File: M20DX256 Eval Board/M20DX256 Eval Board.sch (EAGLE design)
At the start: 20 parts, among them J1 M52-040000S0545, J2 20_PIN, J3 20_PIN, SW1 KMR211G, U1 MK20DX256VLH7, Y1 8MHz, Y2 32.768kHz, 12.5pF

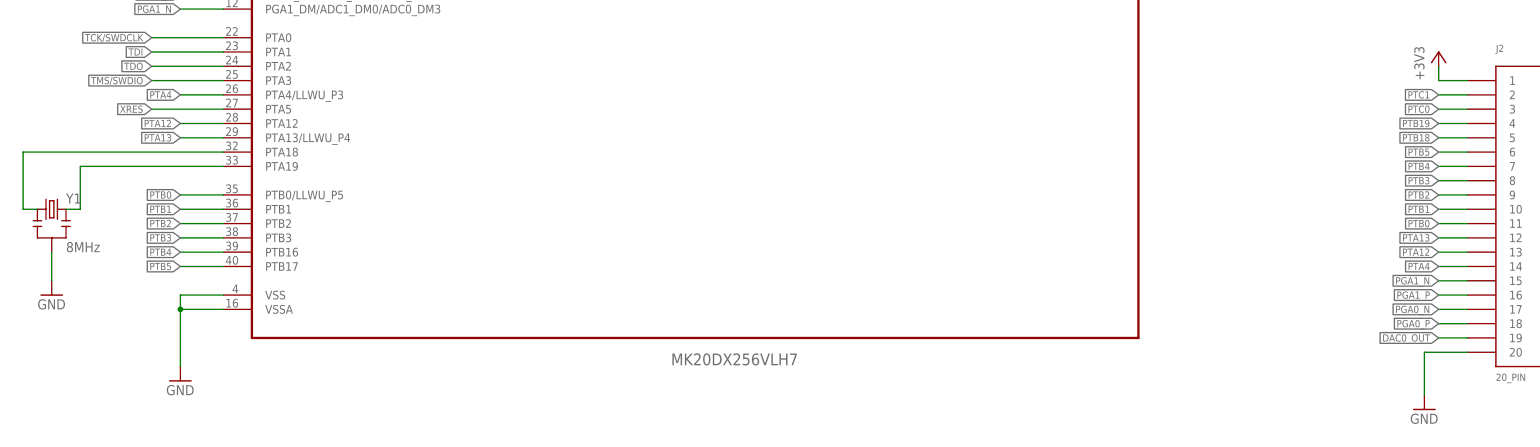
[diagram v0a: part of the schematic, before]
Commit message: Place the component on the board
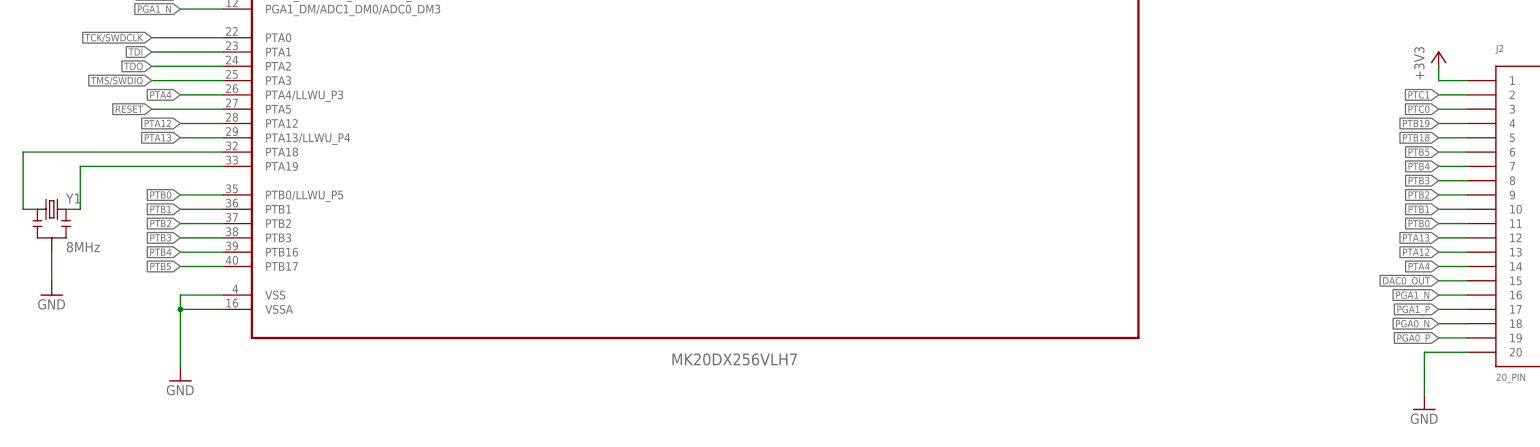
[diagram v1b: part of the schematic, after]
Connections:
- removed net XRES: U1A.PTA5
- net DAC0_OUT: now also J2.15; no longer J2.19
- net PGA0_N: now also J2.18; no longer J2.17
- net PGA0_P: now also J2.19; no longer J2.18
- net PGA1_N: now also J2.16; no longer J2.15
- net PGA1_P: now also J2.17; no longer J2.16
- net RESET: now also U1A.PTA5
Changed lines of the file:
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@@
-</segment>
-</net>
-<net name="XRES" class="0">
-<segment>
-<pinref part="U1" gate="A" pin="PTA5"/>
-<wire x1="137.16" y1="185.42" x2="124.46" y2="185.42" width="0.1524" layer="91"/>
-<label x="124.46" y="185.42" size="1.27" layer="95" rot="R180" xref="yes"/>
 </segment>
 </net>
@@
 </segment>
 <segment>
-<wire x1="358.14" y1="154.94" x2="353.06" y2="154.94" width="0.1524" layer="91"/>
-<label x="353.06" y="154.94" size="1.27" layer="95" rot="R180" xref="yes"/>
-<pinref part="J2" gate="G$1" pin="15"/>
+<wire x1="358.14" y1="152.4" x2="353.06" y2="152.4" width="0.1524" layer="91"/>
+<label x="353.06" y="152.4" size="1.27" layer="95" rot="R180" xref="yes"/>
+<pinref part="J2" gate="G$1" pin="16"/>
 </segment>
 </net>
@@
 </segment>
 <segment>
-<wire x1="358.14" y1="152.4" x2="353.06" y2="152.4" width="0.1524" layer="91"/>
-<label x="353.06" y="152.4" size="1.27" layer="95" rot="R180" xref="yes"/>
-<pinref part="J2" gate="G$1" pin="16"/>
+<wire x1="358.14" y1="149.86" x2="353.06" y2="149.86" width="0.1524" layer="91"/>
+<label x="353.06" y="149.86" size="1.27" layer="95" rot="R180" xref="yes"/>
+<pinref part="J2" gate="G$1" pin="17"/>
 </segment>
 </net>
@@
 </segment>
 <segment>
-<wire x1="358.14" y1="149.86" x2="353.06" y2="149.86" width="0.1524" layer="91"/>
-<label x="353.06" y="149.86" size="1.27" layer="95" rot="R180" xref="yes"/>
-<pinref part="J2" gate="G$1" pin="17"/>
+<wire x1="358.14" y1="147.32" x2="353.06" y2="147.32" width="0.1524" layer="91"/>
+<label x="353.06" y="147.32" size="1.27" layer="95" rot="R180" xref="yes"/>
+<pinref part="J2" gate="G$1" pin="18"/>
 </segment>
 </net>
@@
 </segment>
 <segment>
-<wire x1="358.14" y1="147.32" x2="353.06" y2="147.32" width="0.1524" layer="91"/>
-<label x="353.06" y="147.32" size="1.27" layer="95" rot="R180" xref="yes"/>
-<pinref part="J2" gate="G$1" pin="18"/>
+<wire x1="358.14" y1="144.78" x2="353.06" y2="144.78" width="0.1524" layer="91"/>
+<label x="353.06" y="144.78" size="1.27" layer="95" rot="R180" xref="yes"/>
+<pinref part="J2" gate="G$1" pin="19"/>
 </segment>
 </net>
@@
 <label x="347.98" y="226.06" size="1.27" layer="95" rot="R180" xref="yes"/>
 </segment>
+<segment>
+<pinref part="U1" gate="A" pin="PTA5"/>
+<wire x1="137.16" y1="185.42" x2="124.46" y2="185.42" width="0.1524" layer="91"/>
+<label x="124.46" y="185.42" size="1.27" layer="95" rot="R180" xref="yes"/>
+</segment>
 </net>
 <net name="N$7" class="0">
@@
 </segment>
 <segment>
-<pinref part="J2" gate="G$1" pin="19"/>
-<wire x1="358.14" y1="144.78" x2="353.06" y2="144.78" width="0.1524" layer="91"/>
-<label x="353.06" y="144.78" size="1.27" layer="95" rot="R180" xref="yes"/>
-</segment>
-</net>
+<wire x1="358.14" y1="154.94" x2="353.06" y2="154.94" width="0.1524" layer="91"/>
+<label x="353.06" y="154.94" size="1.27" layer="95" rot="R180" xref="yes"/>
+<pinref part="J2" gate="G$1" pin="15"/>
+</segment>
+</net>

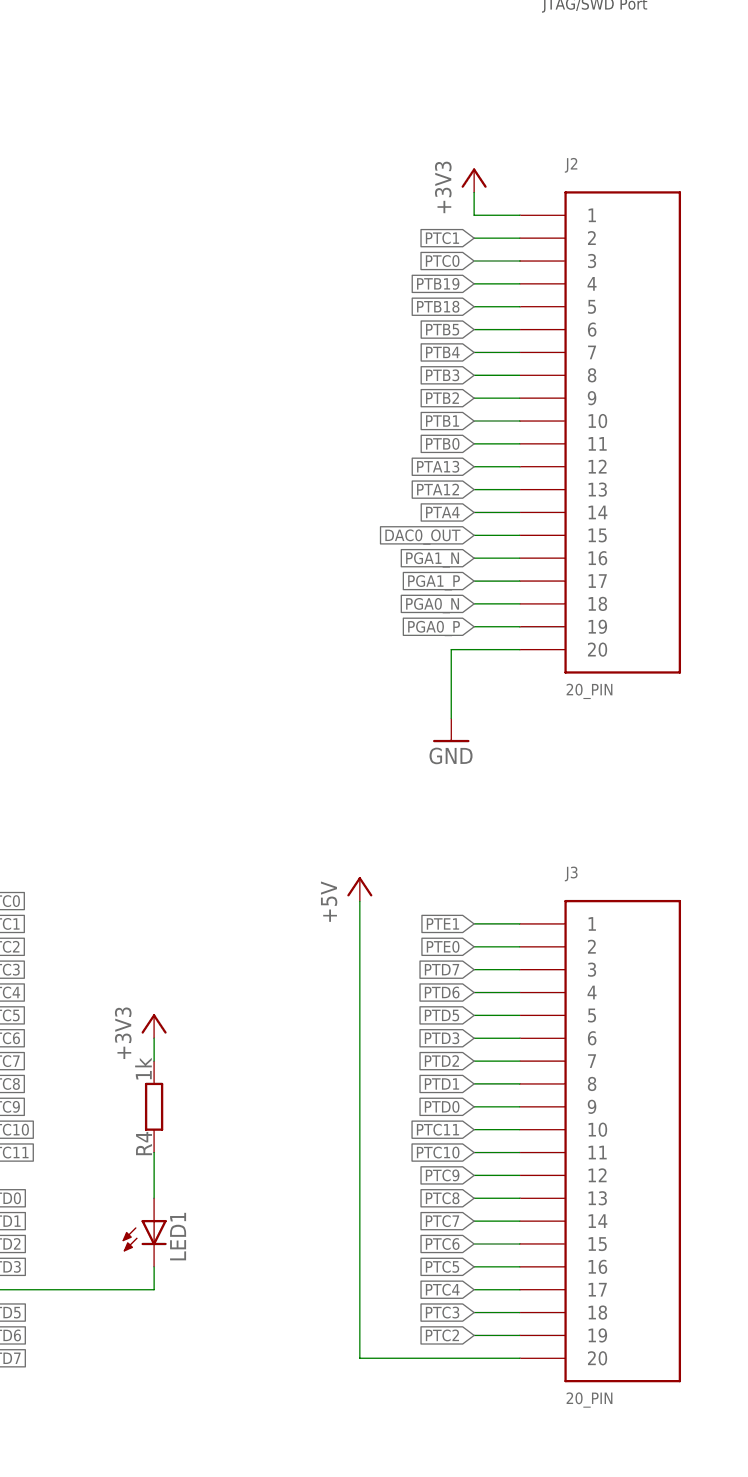
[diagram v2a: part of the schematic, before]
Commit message: Route the power supply +5V
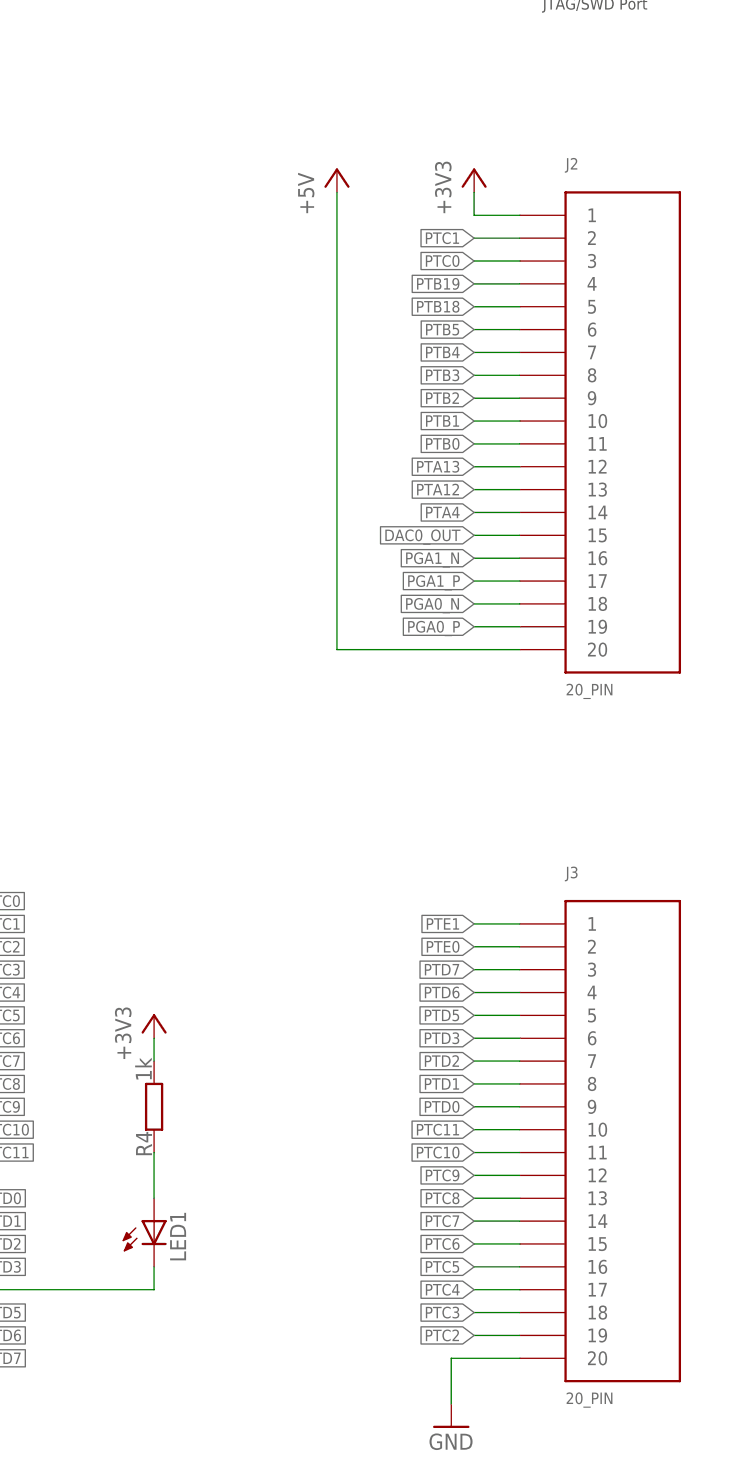
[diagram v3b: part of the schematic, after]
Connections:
- net +5V: now also J2.20; no longer J3.20
- net GND: now also J3.20; no longer J2.20
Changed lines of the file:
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@@
 <part name="J3" library="con-custom" deviceset="20_PIN" device=""/>
 <part name="+3V8" library="supply1" deviceset="+3V3" device=""/>
-<part name="P+3" library="supply1" deviceset="+5V" device=""/>
-<part name="GND8" library="supply1" deviceset="GND" device=""/>
 <part name="R3" library="rcl" deviceset="R-EU_" device="R0603" value="10k"/>
 <part name="C7" library="rcl" deviceset="C-EU" device="C0603" value="0.1uF"/>
@@
 <part name="R4" library="rcl" deviceset="R-EU_" device="R0603" value="1k"/>
 <part name="+3V10" library="supply1" deviceset="+3V3" device=""/>
+<part name="GND11" library="supply1" deviceset="GND" device=""/>
+<part name="P+4" library="supply1" deviceset="+5V" device=""/>
 </parts>
 <sheets>
@@
 <instance part="J3" gate="G$1" x="370.84" y="88.9"/>
 <instance part="+3V8" gate="G$1" x="353.06" y="195.58"/>
-<instance part="P+3" gate="1" x="340.36" y="116.84"/>
-<instance part="GND8" gate="1" x="350.52" y="132.08"/>
 <instance part="R3" gate="G$1" x="15.24" y="165.1" rot="R90"/>
 <instance part="C7" gate="G$1" x="15.24" y="152.4"/>
@@
 </instance>
 <instance part="+3V10" gate="G$1" x="317.5" y="101.6"/>
+<instance part="GND11" gate="1" x="350.52" y="55.88"/>
+<instance part="P+4" gate="1" x="337.82" y="195.58"/>
 </instances>
 <busses>
@@
 </segment>
 <segment>
-<pinref part="GND8" gate="1" pin="GND"/>
-<wire x1="350.52" y1="134.62" x2="350.52" y2="142.24" width="0.1524" layer="91"/>
-<pinref part="J2" gate="G$1" pin="20"/>
-<wire x1="350.52" y1="142.24" x2="358.14" y2="142.24" width="0.1524" layer="91"/>
-</segment>
-<segment>
 <pinref part="C7" gate="G$1" pin="2"/>
 <pinref part="GND9" gate="1" pin="GND"/>
@@
 <pinref part="GND10" gate="1" pin="GND"/>
 </segment>
+<segment>
+<pinref part="J3" gate="G$1" pin="20"/>
+<pinref part="GND11" gate="1" pin="GND"/>
+<wire x1="358.14" y1="63.5" x2="350.52" y2="63.5" width="0.1524" layer="91"/>
+<wire x1="350.52" y1="63.5" x2="350.52" y2="58.42" width="0.1524" layer="91"/>
+</segment>
 </net>
 <net name="+5V" class="0">
@@
 </segment>
 <segment>
-<pinref part="P+3" gate="1" pin="+5V"/>
-<wire x1="340.36" y1="114.3" x2="340.36" y2="63.5" width="0.1524" layer="91"/>
-<pinref part="J3" gate="G$1" pin="20"/>
-<wire x1="358.14" y1="63.5" x2="340.36" y2="63.5" width="0.1524" layer="91"/>
+<pinref part="J2" gate="G$1" pin="20"/>
+<pinref part="P+4" gate="1" pin="+5V"/>
+<wire x1="358.14" y1="142.24" x2="337.82" y2="142.24" width="0.1524" layer="91"/>
+<wire x1="337.82" y1="142.24" x2="337.82" y2="193.04" width="0.1524" layer="91"/>
 </segment>
 </net>

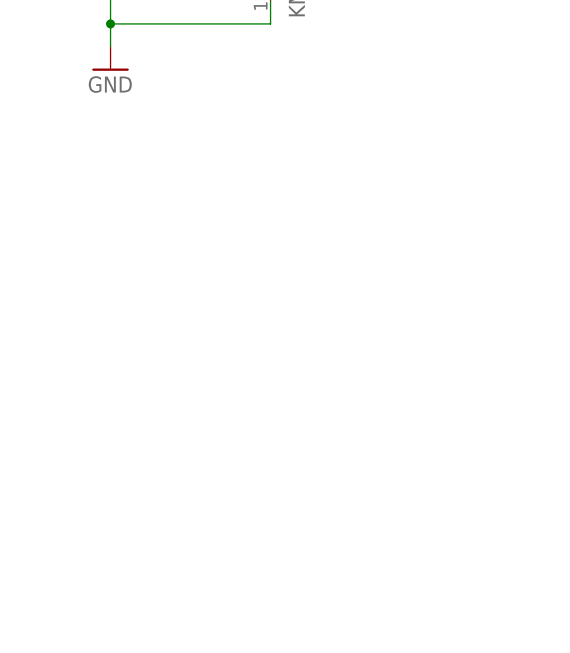
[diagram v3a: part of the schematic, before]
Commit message: Add LED power to the schematic and route the board
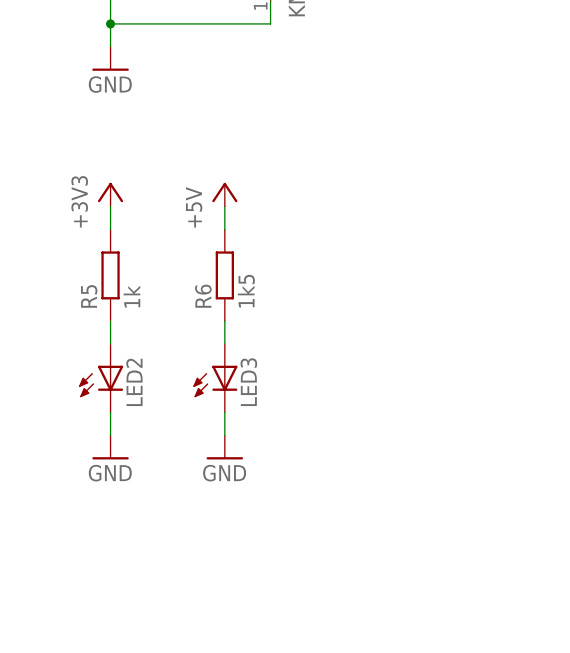
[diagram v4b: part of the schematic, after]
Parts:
- added LED2, LED3: (no value), led:LEDCHIP-LED0603
- added R5: 1k, rcl:R-EU_R0603
- added R6: 1k5, rcl:R-EU_R0603
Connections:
- new net N$10: LED2.A, R5.1
- new net N$9: LED3.A, R6.1
- net +3V3: now also R5.2
- net +5V: now also R6.2
- net GND: now also LED2.C, LED3.C
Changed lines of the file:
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@@
 <part name="GND11" library="supply1" deviceset="GND" device=""/>
 <part name="P+4" library="supply1" deviceset="+5V" device=""/>
+<part name="+3V11" library="supply1" deviceset="+3V3" device=""/>
+<part name="R5" library="rcl" deviceset="R-EU_" device="R0603" value="1k"/>
+<part name="GND8" library="supply1" deviceset="GND" device=""/>
+<part name="GND12" library="supply1" deviceset="GND" device=""/>
+<part name="R6" library="rcl" deviceset="R-EU_" device="R0603" value="1k5"/>
+<part name="P+3" library="supply1" deviceset="+5V" device=""/>
+<part name="LED2" library="led" deviceset="LED" device="CHIP-LED0603"/>
+<part name="LED3" library="led" deviceset="LED" device="CHIP-LED0603"/>
 </parts>
 <sheets>
@@
 <instance part="GND11" gate="1" x="350.52" y="55.88"/>
 <instance part="P+4" gate="1" x="337.82" y="195.58"/>
+<instance part="+3V11" gate="G$1" x="15.24" y="124.46"/>
+<instance part="R5" gate="G$1" x="15.24" y="114.3" rot="R90"/>
+<instance part="GND8" gate="1" x="15.24" y="93.98"/>
+<instance part="GND12" gate="1" x="27.94" y="93.98"/>
+<instance part="R6" gate="G$1" x="27.94" y="114.3" rot="R90"/>
+<instance part="P+3" gate="1" x="27.94" y="124.46"/>
+<instance part="LED2" gate="G$1" x="15.24" y="104.14"/>
+<instance part="LED3" gate="G$1" x="27.94" y="104.14"/>
 </instances>
 <busses>
@@
 <pinref part="+3V10" gate="G$1" pin="+3V3"/>
 <wire x1="317.5" y1="96.52" x2="317.5" y2="99.06" width="0.1524" layer="91"/>
+</segment>
+<segment>
+<pinref part="R5" gate="G$1" pin="2"/>
+<pinref part="+3V11" gate="G$1" pin="+3V3"/>
+<wire x1="15.24" y1="119.38" x2="15.24" y2="121.92" width="0.1524" layer="91"/>
 </segment>
 </net>
@@
 <wire x1="350.52" y1="63.5" x2="350.52" y2="58.42" width="0.1524" layer="91"/>
 </segment>
+<segment>
+<pinref part="GND8" gate="1" pin="GND"/>
+<pinref part="LED2" gate="G$1" pin="C"/>
+<wire x1="15.24" y1="96.52" x2="15.24" y2="99.06" width="0.1524" layer="91"/>
+</segment>
+<segment>
+<pinref part="GND12" gate="1" pin="GND"/>
+<pinref part="LED3" gate="G$1" pin="C"/>
+<wire x1="27.94" y1="96.52" x2="27.94" y2="99.06" width="0.1524" layer="91"/>
+</segment>
 </net>
 <net name="+5V" class="0">
@@
 <wire x1="358.14" y1="142.24" x2="337.82" y2="142.24" width="0.1524" layer="91"/>
 <wire x1="337.82" y1="142.24" x2="337.82" y2="193.04" width="0.1524" layer="91"/>
+</segment>
+<segment>
+<pinref part="R6" gate="G$1" pin="2"/>
+<pinref part="P+3" gate="1" pin="+5V"/>
+<wire x1="27.94" y1="119.38" x2="27.94" y2="121.92" width="0.1524" layer="91"/>
 </segment>
 </net>
@@
 </segment>
 </net>
+<net name="N$9" class="0">
+<segment>
+<pinref part="LED3" gate="G$1" pin="A"/>
+<pinref part="R6" gate="G$1" pin="1"/>
+<wire x1="27.94" y1="106.68" x2="27.94" y2="109.22" width="0.1524" layer="91"/>
+</segment>
+</net>
+<net name="N$10" class="0">
+<segment>
+<pinref part="LED2" gate="G$1" pin="A"/>
+<pinref part="R5" gate="G$1" pin="1"/>
+<wire x1="15.24" y1="106.68" x2="15.24" y2="109.22" width="0.1524" layer="91"/>
+</segment>
+</net>
